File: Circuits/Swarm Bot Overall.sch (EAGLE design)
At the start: 7 parts, among them IC1 MEGA164P/324P/644P-AU, IC2 MCP73831

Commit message: Finished Charger?
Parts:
- added 10K, 20K: (no value), resistor:R-US_0204/5
- added R2, R3, R4, R5: 20k, resistor:R-US_0204/5
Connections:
- new net CHARGESTATE: R4.1, R5.2
- new net N$6: IC2.STAT, R4.2
- new net VOLTAGEDETECT: R2.1, R3.2
- net +5V: now also R2.2
- net GND: now also R3.1, R5.1
- net N$3: now also 10K.1, 20K.2; no longer IC2.STAT
- net V+: now also 10K.2
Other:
- moved on the sheet: BATTERY-1, BATTERY-2, C1
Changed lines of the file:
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@@
 <part name="FTDI" library="con-amp-quick" deviceset="M03S" device=""/>
 <part name="GND3" library="supply1" deviceset="GND" device=""/>
+<part name="R2" library="resistor" deviceset="R-US_" device="0204/5" value="20k"/>
+<part name="R3" library="resistor" deviceset="R-US_" device="0204/5" value="20k"/>
+<part name="R4" library="resistor" deviceset="R-US_" device="0204/5" value="20k"/>
+<part name="R5" library="resistor" deviceset="R-US_" device="0204/5" value="20k"/>
+<part name="10K" library="resistor" deviceset="R-US_" device="0204/5"/>
+<part name="20K" library="resistor" deviceset="R-US_" device="0204/5"/>
 </parts>
 <sheets>
@@
 <instance part="IC2" gate="G$1" x="-104.14" y="165.1"/>
 <instance part="R1" gate="G$1" x="-88.9" y="165.1"/>
-<instance part="C1" gate="G$1" x="-124.46" y="157.48"/>
-<instance part="GND2" gate="1" x="-83.82" y="144.78"/>
-<instance part="P+1" gate="1" x="-124.46" y="175.26"/>
+<instance part="C1" gate="G$1" x="-119.38" y="157.48"/>
+<instance part="GND2" gate="1" x="-83.82" y="139.7"/>
+<instance part="P+1" gate="1" x="-119.38" y="187.96"/>
 <instance part="C2" gate="G$1" x="-76.2" y="162.56"/>
-<instance part="P+2" gate="1" x="-76.2" y="177.8"/>
-<instance part="BATTERY" gate="-1" x="-60.96" y="167.64" rot="R180"/>
-<instance part="BATTERY" gate="-2" x="-60.96" y="170.18" rot="R180"/>
+<instance part="P+2" gate="1" x="-76.2" y="187.96"/>
+<instance part="BATTERY" gate="-1" x="-55.88" y="149.86" rot="R180"/>
+<instance part="BATTERY" gate="-2" x="-55.88" y="170.18" rot="R180"/>
 <instance part="FTDI" gate="-1" x="226.06" y="73.66" rot="R180"/>
 <instance part="FTDI" gate="-2" x="226.06" y="76.2" rot="R180"/>
 <instance part="FTDI" gate="-3" x="226.06" y="78.74" rot="R180"/>
 <instance part="GND3" gate="1" x="218.44" y="68.58"/>
+<instance part="R2" gate="G$1" x="-124.46" y="167.64"/>
+<instance part="R3" gate="G$1" x="-134.62" y="167.64"/>
+<instance part="R4" gate="G$1" x="-139.7" y="162.56"/>
+<instance part="R5" gate="G$1" x="-149.86" y="162.56"/>
+<instance part="10K" gate="G$1" x="-66.04" y="165.1" rot="R90"/>
+<instance part="20K" gate="G$1" x="-66.04" y="154.94" rot="R90"/>
 </instances>
 <busses>
@@
 <wire x1="-93.98" y1="160.02" x2="-83.82" y2="160.02" width="0.1524" layer="91"/>
 <wire x1="-83.82" y1="165.1" x2="-83.82" y2="160.02" width="0.1524" layer="91"/>
-<wire x1="-83.82" y1="160.02" x2="-83.82" y2="152.4" width="0.1524" layer="91"/>
-<wire x1="-83.82" y1="152.4" x2="-124.46" y2="152.4" width="0.1524" layer="91"/>
+<wire x1="-83.82" y1="160.02" x2="-83.82" y2="149.86" width="0.1524" layer="91"/>
+<wire x1="-83.82" y1="149.86" x2="-83.82" y2="142.24" width="0.1524" layer="91"/>
+<junction x="-83.82" y="160.02"/>
+<junction x="-83.82" y="149.86"/>
+<pinref part="GND2" gate="1" pin="GND"/>
+<wire x1="-83.82" y1="149.86" x2="-76.2" y2="149.86" width="0.1524" layer="91"/>
+<pinref part="C2" gate="G$1" pin="2"/>
+<wire x1="-76.2" y1="149.86" x2="-76.2" y2="157.48" width="0.1524" layer="91"/>
 <pinref part="C1" gate="G$1" pin="2"/>
-<wire x1="-83.82" y1="152.4" x2="-83.82" y2="147.32" width="0.1524" layer="91"/>
-<junction x="-83.82" y="160.02"/>
-<junction x="-83.82" y="152.4"/>
-<pinref part="GND2" gate="1" pin="GND"/>
-<wire x1="-83.82" y1="152.4" x2="-76.2" y2="152.4" width="0.1524" layer="91"/>
-<pinref part="C2" gate="G$1" pin="2"/>
-<wire x1="-76.2" y1="152.4" x2="-76.2" y2="157.48" width="0.1524" layer="91"/>
-<wire x1="-76.2" y1="152.4" x2="-68.58" y2="152.4" width="0.1524" layer="91"/>
-<wire x1="-68.58" y1="167.64" x2="-68.58" y2="152.4" width="0.1524" layer="91"/>
+<wire x1="-119.38" y1="152.4" x2="-119.38" y2="149.86" width="0.1524" layer="91"/>
+<wire x1="-119.38" y1="149.86" x2="-83.82" y2="149.86" width="0.1524" layer="91"/>
+<pinref part="R3" gate="G$1" pin="1"/>
+<wire x1="-139.7" y1="167.64" x2="-154.94" y2="167.64" width="0.1524" layer="91"/>
+<wire x1="-154.94" y1="167.64" x2="-154.94" y2="162.56" width="0.1524" layer="91"/>
+<wire x1="-154.94" y1="162.56" x2="-154.94" y2="149.86" width="0.1524" layer="91"/>
+<wire x1="-154.94" y1="149.86" x2="-119.38" y2="149.86" width="0.1524" layer="91"/>
+<junction x="-119.38" y="149.86"/>
+<pinref part="R5" gate="G$1" pin="1"/>
+<junction x="-154.94" y="162.56"/>
 <pinref part="BATTERY" gate="-1" pin="S"/>
-<wire x1="-66.04" y1="167.64" x2="-68.58" y2="167.64" width="0.1524" layer="91"/>
+<wire x1="-76.2" y1="149.86" x2="-60.96" y2="149.86" width="0.1524" layer="91"/>
+<junction x="-76.2" y="149.86"/>
 </segment>
 <segment>
@@
 </segment>
 </net>
-<net name="N$3" class="0">
-<segment>
-<pinref part="IC2" gate="G$1" pin="STAT"/>
-<wire x1="-114.3" y1="162.56" x2="-142.24" y2="162.56" width="0.1524" layer="91"/>
-</segment>
-</net>
 <net name="+5V" class="0">
 <segment>
 <pinref part="IC2" gate="G$1" pin="VDD"/>
 <pinref part="C1" gate="G$1" pin="1"/>
-<wire x1="-114.3" y1="167.64" x2="-124.46" y2="167.64" width="0.1524" layer="91"/>
-<wire x1="-124.46" y1="167.64" x2="-124.46" y2="160.02" width="0.1524" layer="91"/>
-<wire x1="-124.46" y1="167.64" x2="-124.46" y2="172.72" width="0.1524" layer="91"/>
-<junction x="-124.46" y="167.64"/>
+<wire x1="-114.3" y1="167.64" x2="-119.38" y2="167.64" width="0.1524" layer="91"/>
+<wire x1="-119.38" y1="167.64" x2="-119.38" y2="160.02" width="0.1524" layer="91"/>
+<wire x1="-119.38" y1="167.64" x2="-119.38" y2="185.42" width="0.1524" layer="91"/>
+<junction x="-119.38" y="167.64"/>
 <pinref part="P+1" gate="1" pin="+5V"/>
+<pinref part="R2" gate="G$1" pin="2"/>
 </segment>
 </net>
@@
 <wire x1="-76.2" y1="170.18" x2="-93.98" y2="170.18" width="0.1524" layer="91"/>
 <wire x1="-76.2" y1="170.18" x2="-66.04" y2="170.18" width="0.1524" layer="91"/>
-<wire x1="-76.2" y1="170.18" x2="-76.2" y2="175.26" width="0.1524" layer="91"/>
+<wire x1="-66.04" y1="170.18" x2="-60.96" y2="170.18" width="0.1524" layer="91"/>
+<wire x1="-76.2" y1="170.18" x2="-76.2" y2="185.42" width="0.1524" layer="91"/>
 <junction x="-76.2" y="170.18"/>
 <pinref part="P+2" gate="1" pin="V+"/>
 <pinref part="BATTERY" gate="-2" pin="S"/>
+<pinref part="10K" gate="G$1" pin="2"/>
+<junction x="-66.04" y="170.18"/>
 </segment>
 </net>
@@
 </segment>
 </net>
+<net name="VOLTAGEDETECT" class="0">
+<segment>
+<pinref part="R2" gate="G$1" pin="1"/>
+<pinref part="R3" gate="G$1" pin="2"/>
+<wire x1="-129.54" y1="167.64" x2="-129.54" y2="177.8" width="0.1524" layer="91"/>
+<label x="-129.54" y="170.18" size="1.778" layer="95" rot="R90"/>
+</segment>
+</net>
+<net name="CHARGESTATE" class="0">
+<segment>
+<pinref part="R4" gate="G$1" pin="1"/>
+<pinref part="R5" gate="G$1" pin="2"/>
+<wire x1="-144.78" y1="162.56" x2="-144.78" y2="177.8" width="0.1524" layer="91"/>
+<label x="-144.78" y="170.18" size="1.778" layer="95" rot="R90"/>
+<junction x="-144.78" y="162.56"/>
+</segment>
+</net>
+<net name="N$6" class="0">
+<segment>
+<pinref part="R4" gate="G$1" pin="2"/>
+<pinref part="IC2" gate="G$1" pin="STAT"/>
+<wire x1="-134.62" y1="162.56" x2="-114.3" y2="162.56" width="0.1524" layer="91"/>
+</segment>
+</net>
+<net name="N$3" class="0">
+<segment>
+<pinref part="10K" gate="G$1" pin="1"/>
+<pinref part="20K" gate="G$1" pin="2"/>
+</segment>
+</net>

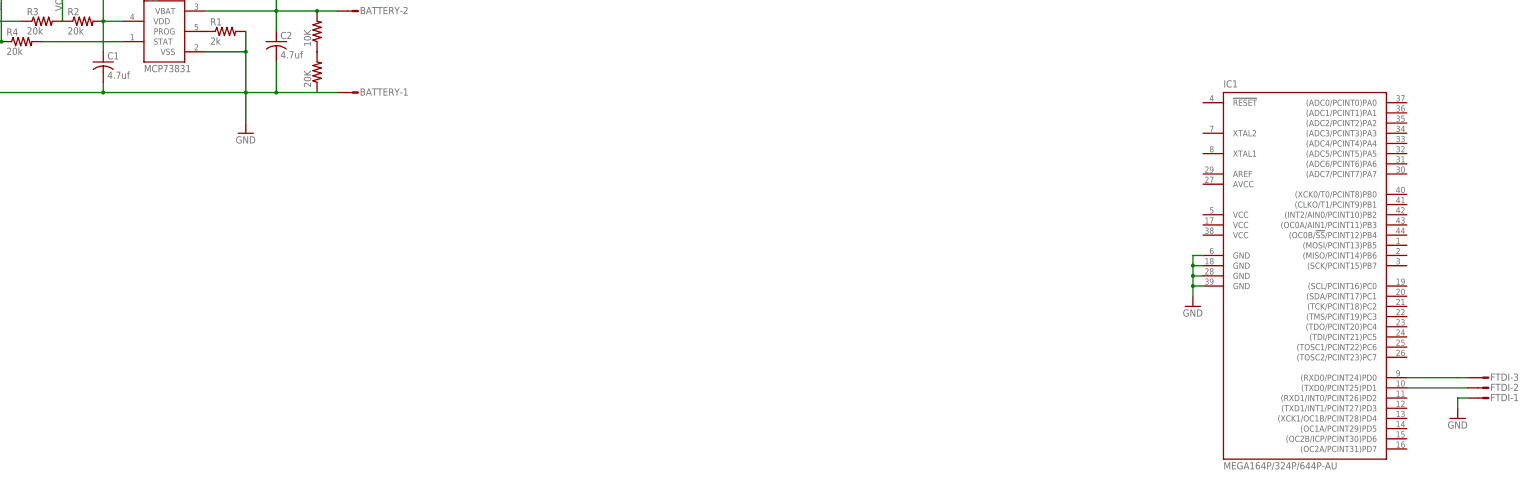
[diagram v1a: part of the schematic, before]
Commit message: 
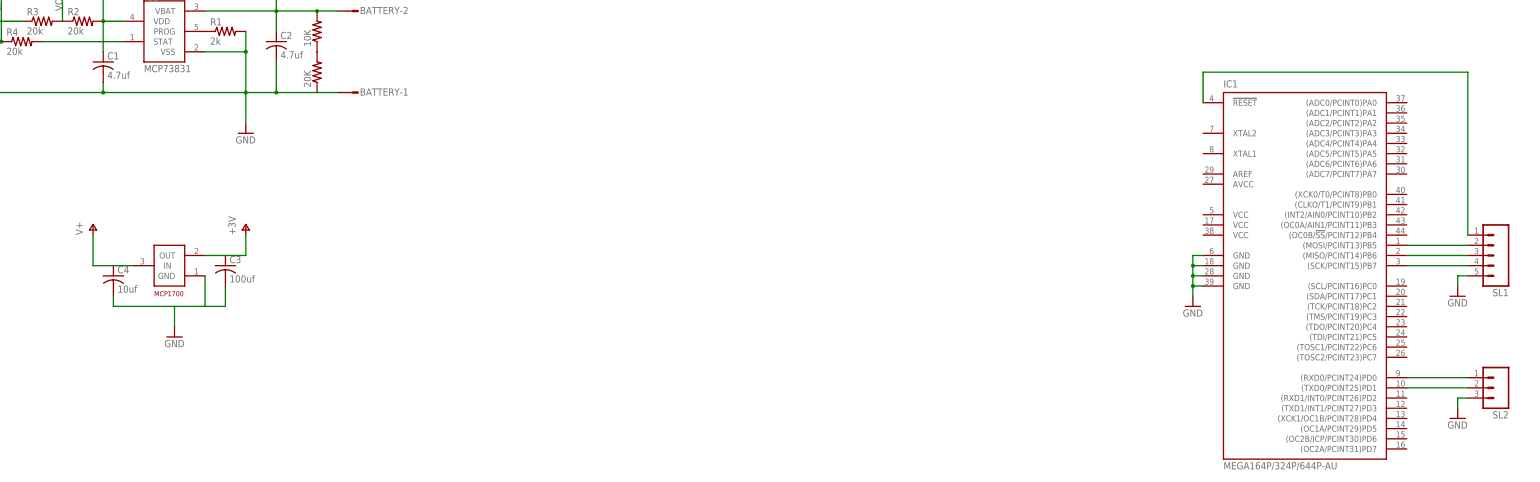
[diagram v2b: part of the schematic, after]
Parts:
- removed FTDI: (no value), con-amp-quick:M03S
- added C3: 100uf, resistor:C-US025-050X050
- added C4: 10uf, resistor:C-US025-050X050
- added SL1: (no value), con-amp-quick:M05
- added SL2: (no value), con-amp-quick:M03
- added U$1: MCP1700T-3002E/TT, SwarmParts:MCP1700T-3002E/TT
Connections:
- new net 3V: U$1.OUT
- new net N$5: IC1.(MOSI/PCINT13)PB5, SL1.2
- new net N$7: IC1.(MISO/PCINT14)PB6, SL1.3
- new net N$8: IC1.(SCK/PCINT15)PB7, SL1.4
- new net N$9: IC1.!RESET, SL1.1
- net GND: now also C3.2, C4.2, SL1.5, SL2.3, U$1.GND; no longer FTDI-1.S
- net N$2: now also SL2.2; no longer FTDI-2.S
- net N$4: now also SL2.1; no longer FTDI-3.S
- net V+: now also U$1.IN
